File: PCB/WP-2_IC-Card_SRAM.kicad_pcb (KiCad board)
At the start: 2 copper layers, 54 x 54 mm, 28 parts, among them J1 SMS-138-01-G-S, SW1 CUS-14TB, U1 AS6C4008

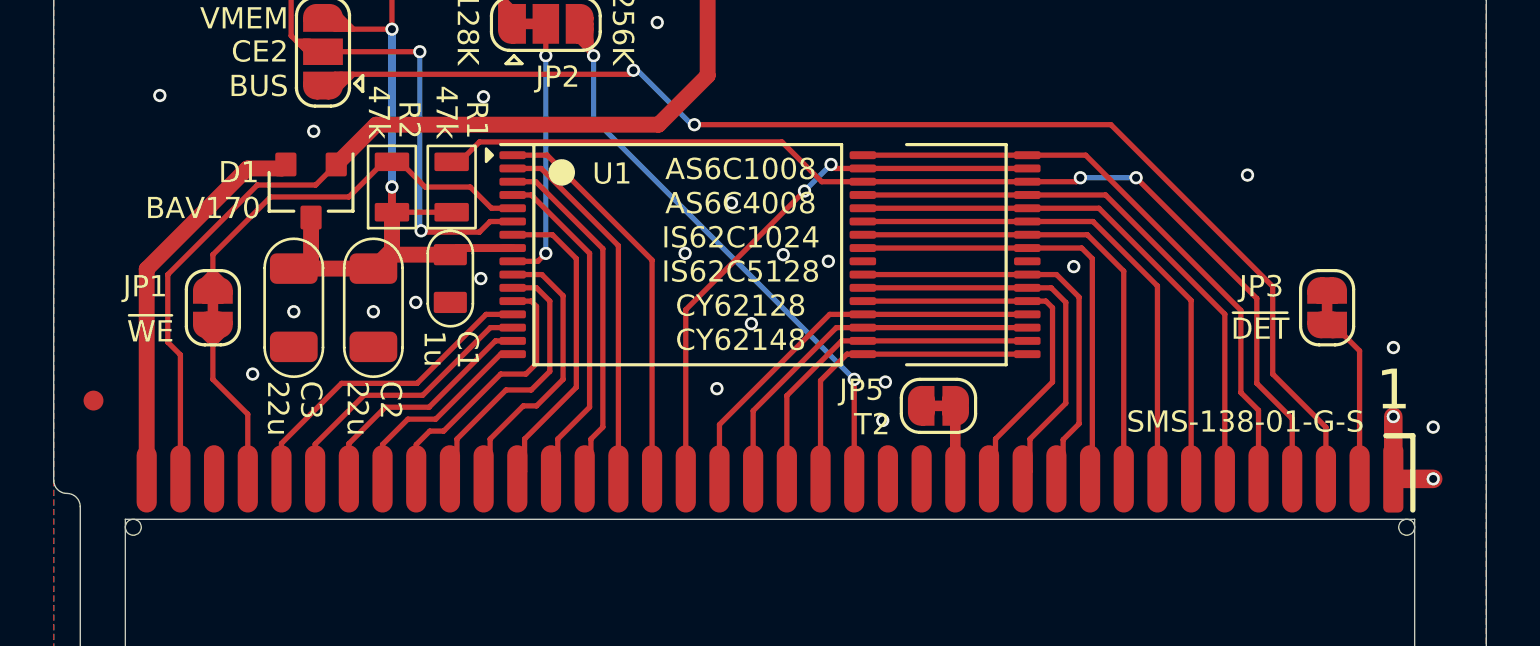
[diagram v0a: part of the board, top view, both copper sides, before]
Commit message: 4 symmetric fiducials
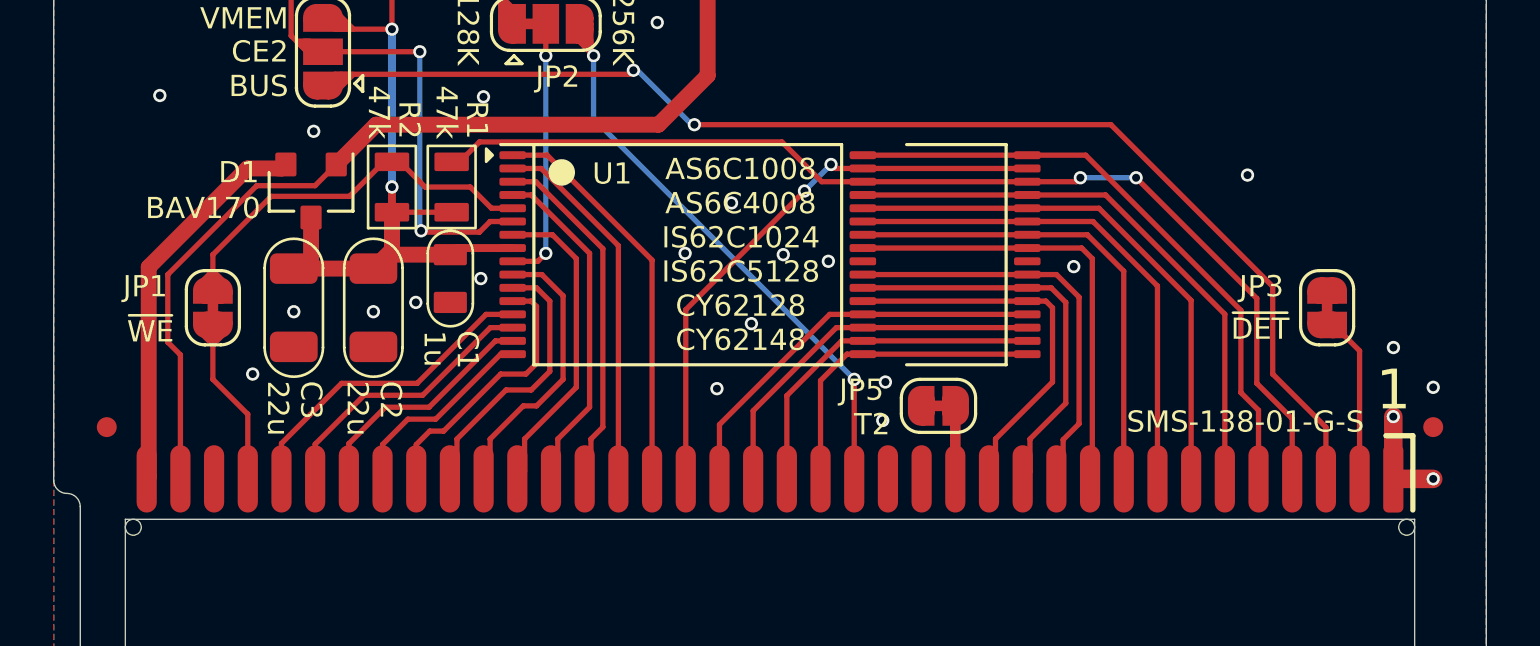
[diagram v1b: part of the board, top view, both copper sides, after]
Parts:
- added REF**: Fiducial_1.5, 000_LOCAL:Fiducial_1.5, F.Cu at (160.9, 110.2)
- moved REF** 1.12 mm to (111.0, 110.2)

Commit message: SRAM battery life, bank sw use vbus
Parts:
- D2: value BAT54CDW -> BAV70S
- moved REF** 1.00 mm to (160.9, 109.2)
- moved REF** 1.00 mm to (111.0, 109.2)
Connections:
- net /A18 renamed /A18_CE2
- net /CE2 renamed /CE2bus
- SW1 pad 3: VMEM -> VBUS
- SW1 pad 4: VMEM -> VBUS
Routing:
- net VBUS: track 14.8 -> 42.3 mm
- net VMEM: track 42.4 -> 26.3 mm
- net /BANK_4: track 11.0 -> 8.31 mm, vias 2 -> 0
- net /CE2bus: track 47.5 -> 49.5 mm
- net +BATT: track 41.8 -> 41.0 mm
- net GND: vias 31 -> 30
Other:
- rule solder_mask_min_width: 0.2 -> 0.22
- board text added: "FOR 128K or 256K CHIP, BRIDGE JP4 CE2-BUS"

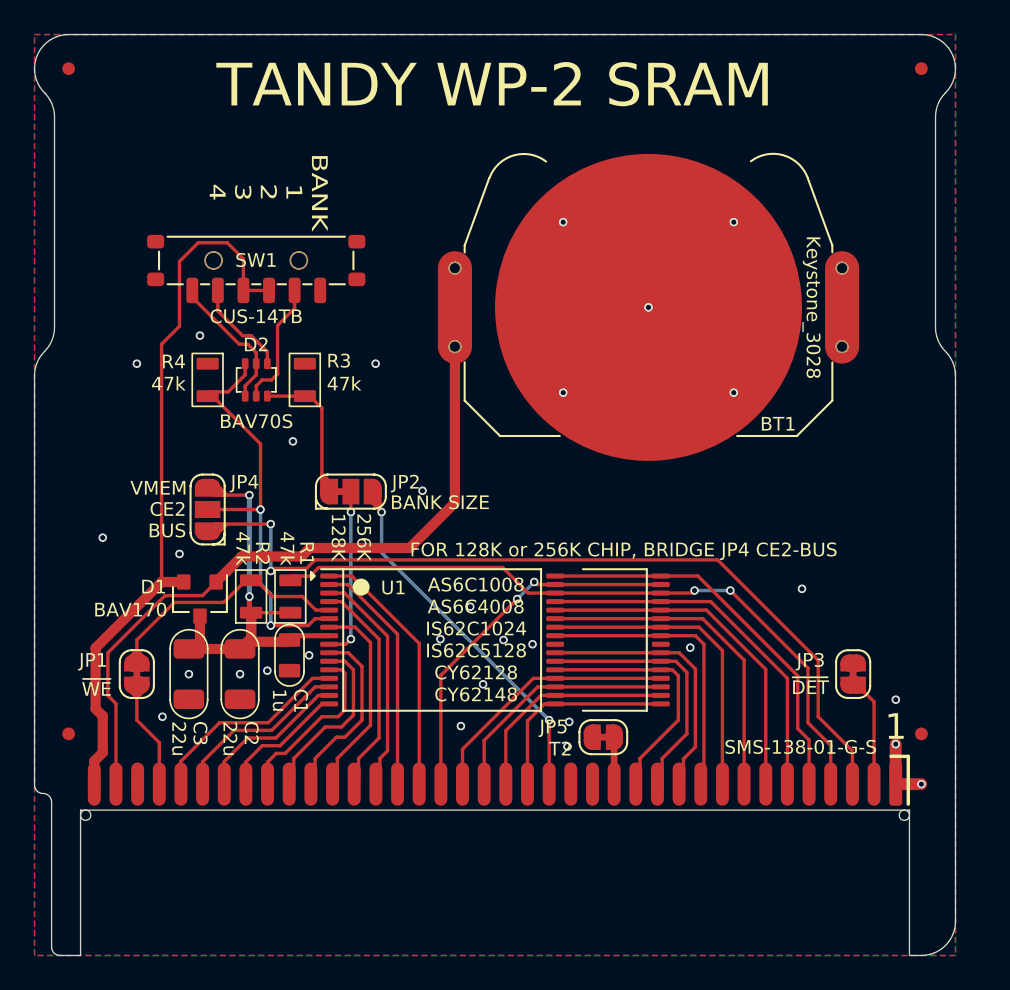
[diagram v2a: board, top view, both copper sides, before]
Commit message: SRAM simpler diodes
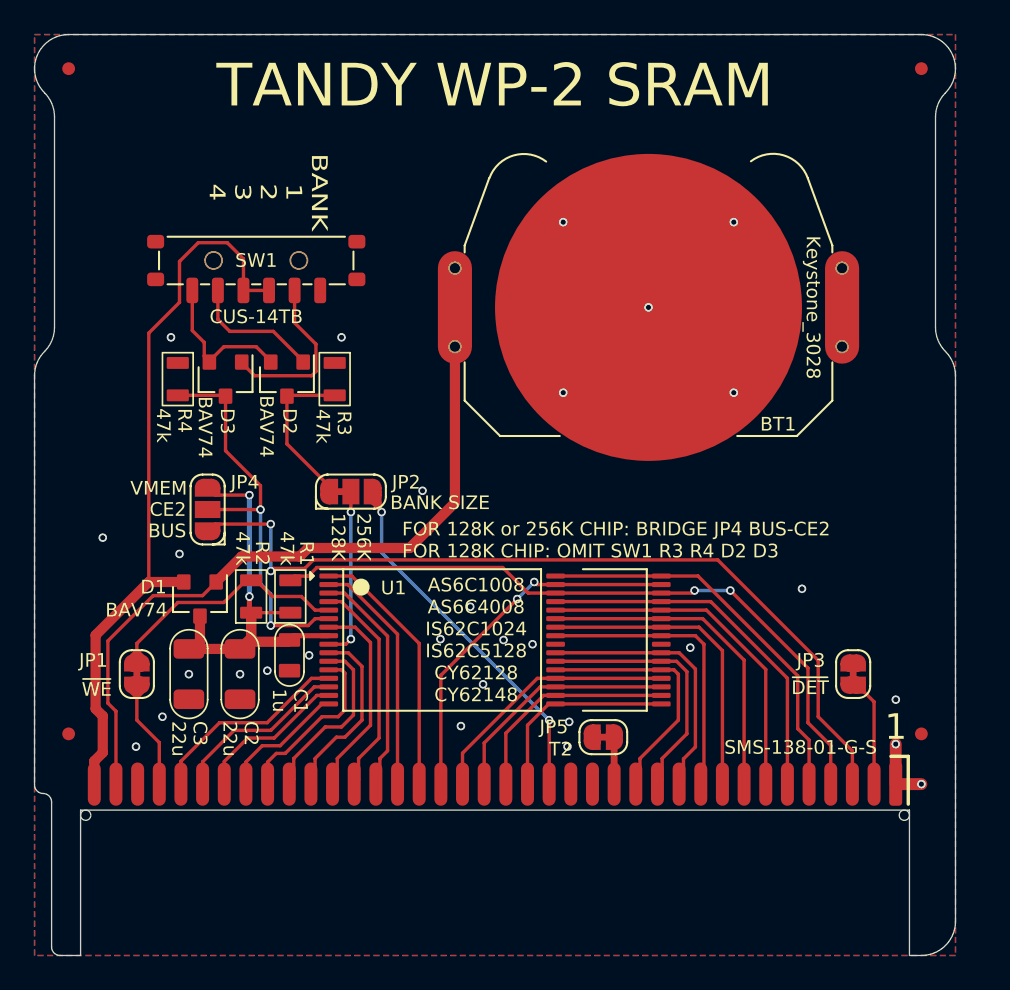
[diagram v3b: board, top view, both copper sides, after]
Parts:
- added D3: BAV74, 000_LOCAL:SOT-23, F.Cu at (120.2, 88.5)
- D1: value BAV170 -> BAV74
- D2: value BAV70S -> BAV74; footprint 000_LOCAL:TSSOP-6-symmetric -> 000_LOCAL:SOT-23
- moved D2 1.80 mm to (123.8, 88.5)
- moved R3 1.75 mm to (126.5, 88.5)
- moved R4 1.75 mm to (117.3, 88.5)
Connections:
- D2 pad 3: /A18_CE2 -> /A17bank
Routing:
- net /BANK_2: track 7.45 -> 10.1 mm
- net /BANK_3: track 5.79 -> 7.76 mm
- net /A18_CE2: track 25.2 -> 24.0 mm
- net /BANK_4: track 8.31 -> 9.17 mm
- net VBUS: track 42.3 -> 43.1 mm
- net /A17bank: track 8.79 -> 9.43 mm
- net GND: vias 30 -> 29
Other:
- board text added: "FOR 128K or 256K CHIP: BRIDGE JP4 BUS-CE2 FOR 128K CHIP: OMIT SW1 R3 R4 D2 D3"
- board text removed: "FOR 128K or 256K CHIP, BRIDGE JP4 CE2-BUS"

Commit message: adhesive tape, pics, tiny routing nudges, tsop2-44 model, grid alignment
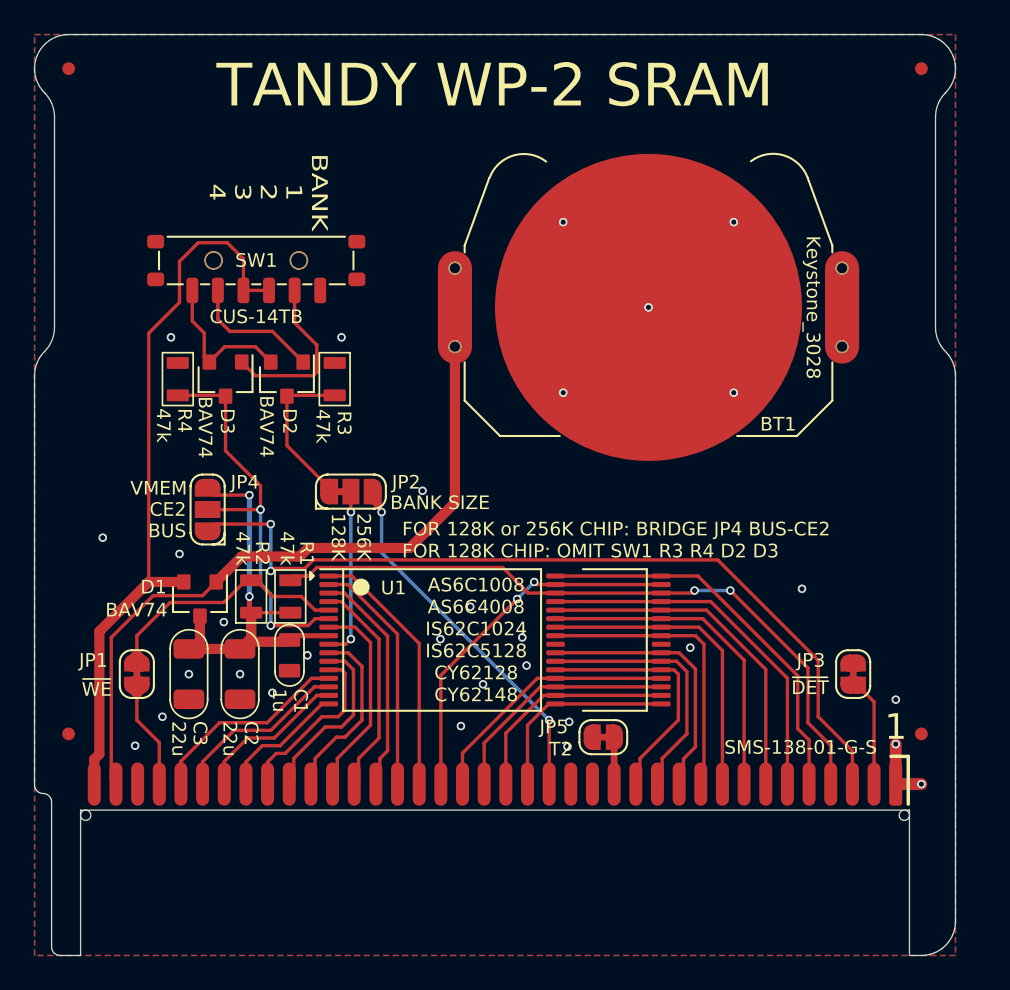
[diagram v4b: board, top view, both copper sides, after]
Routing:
- net GND: vias 29 -> 30
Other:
- board text added: "3MM ADHESIVE TRANSFER TAPE"

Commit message: sram: resistors 100k, silkscreen, pics
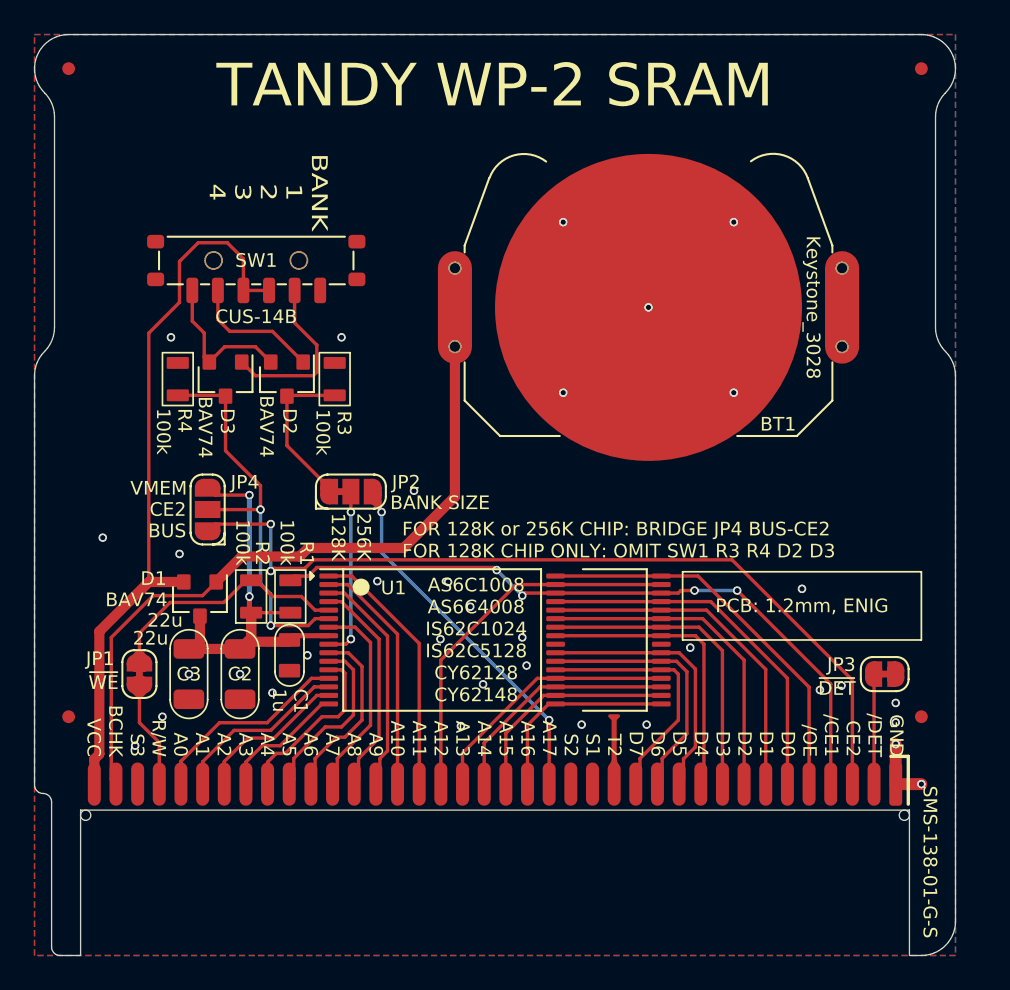
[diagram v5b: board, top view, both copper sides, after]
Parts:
- removed JP5: T2, 000_LOCAL:SolderJumper-2_Bridged
- R1, R2, R3, R4: value 47k -> 100k
- SW1: value CUS-14TB -> CUS-14B
- moved JP3 1.85 mm to (158.8, 105.7), turned to 0 degrees
- moved REF** 1.00 mm to (160.9, 108.2)
- moved REF** 1.00 mm to (111.0, 108.2)
- moved JP1 0.15 mm to (115.1, 105.7)
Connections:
- J1 pad 14: /T2 -> GND
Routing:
- net GND: track 3.85 -> 7.72 mm, vias 30 -> 34
- net /T2: track 2.76 -> 0.00 mm
- net /CE2bus: track 49.5 -> 50.0 mm
- net /A12: track 21.6 -> 22.0 mm, vias 2 -> 0
- net /~{CE1}: track 40.6 -> 40.9 mm, vias 2 -> 4
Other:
- board text added: "FOR 128K or 256K CHIP: BRIDGE JP4 BUS-CE2 FOR 128K CHIP ONLY: OMIT SW1 R3 R4 D2 D3"
- board text added: "GND /DET CE2 /CE1 /OE D0 D1 D2 D3 D4 D5 D6 D7 T2 S1 S2 A17 A16 A15 A14 A13 A12 A11 A10 A9 A8 A7 A6 A5 A4 A3 A2 A1 A0 R/W S3 BCHK VCC"
- board text added: "PCB: 1.2mm, ENIG"
- board text removed: "FOR 128K or 256K CHIP: BRIDGE JP4 BUS-CE2 FOR 128K CHIP: OMIT SW1 R3 R4 D2 D3"

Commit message: silkscreens, board outlines, switch slider, covers fitment, copper to edge
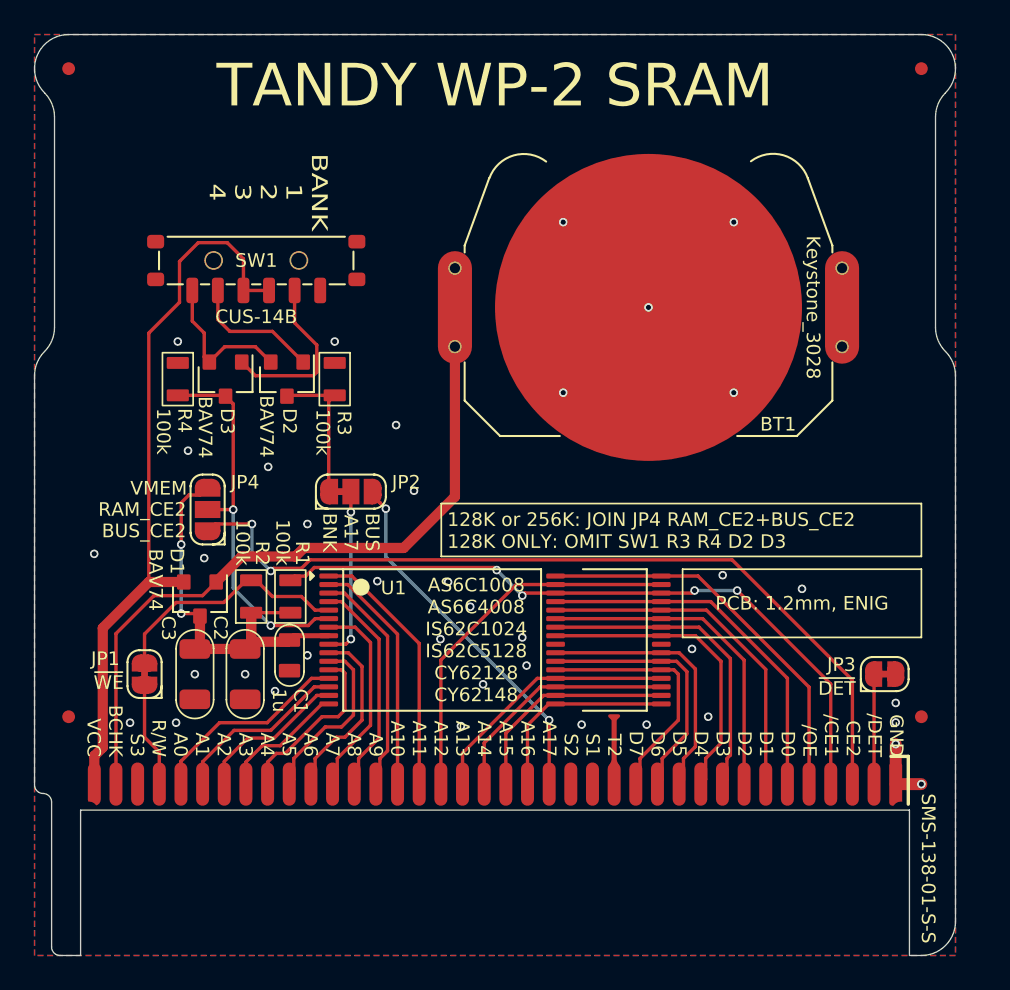
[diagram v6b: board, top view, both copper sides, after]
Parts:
- removed the REF** at (159.9, 114.0)
- removed the REF** at (112.0, 114.0)
- J1: value SMS-138-01-G-S -> SMS-138-01-S-S; footprint 000_LOCAL:SMS-138-01-x-x_pcb_edge -> 000_LOCAL:SMS-138-01-x-S_pcb_edge
- JP2: value BANK SIZE -> A17
- JP4: value CE2 -> RAM_CE2
- N1: value WP-2_IC-Card_Cover_SRAM -> WP-2_IC_Card_Cover_SRAM
- moved C3 0.35 mm to (118.3, 105.8)
- moved C2 0.30 mm to (121.3, 105.8)
- moved JP1 0.30 mm to (115.4, 105.7)
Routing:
- net /A18_CE2: track 24.0 -> 22.4 mm
- net /D4: track 17.2 -> 18.0 mm
- net /A17bank: track 9.43 -> 8.61 mm
- net /CE2bus: track 50.0 -> 49.4 mm
- net GND: vias 34 -> 38
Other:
- board text added: "128K or 256K: JOIN JP4 RAM_CE2+BUS_CE2 128K ONLY: OMIT SW1 R3 R4 D2 D3"
- board text removed: "BOARD OUTLINE"
- board text removed: "FOR 128K or 256K CHIP: BRIDGE JP4 BUS-CE2 FOR 128K CHIP ONLY: OMIT SW1 R3 R4 D2 D3"
